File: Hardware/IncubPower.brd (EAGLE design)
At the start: 50 x 50 mm, 23 parts, among them T1 BT138-V, T2 BT138-V, X1 22-23-2041, X2 MKDSN1,5/2-5,08, X3 MKDSN1,5/2-5,08, X4 22-23-2021, X5 MKDSN1,5/2-5,08

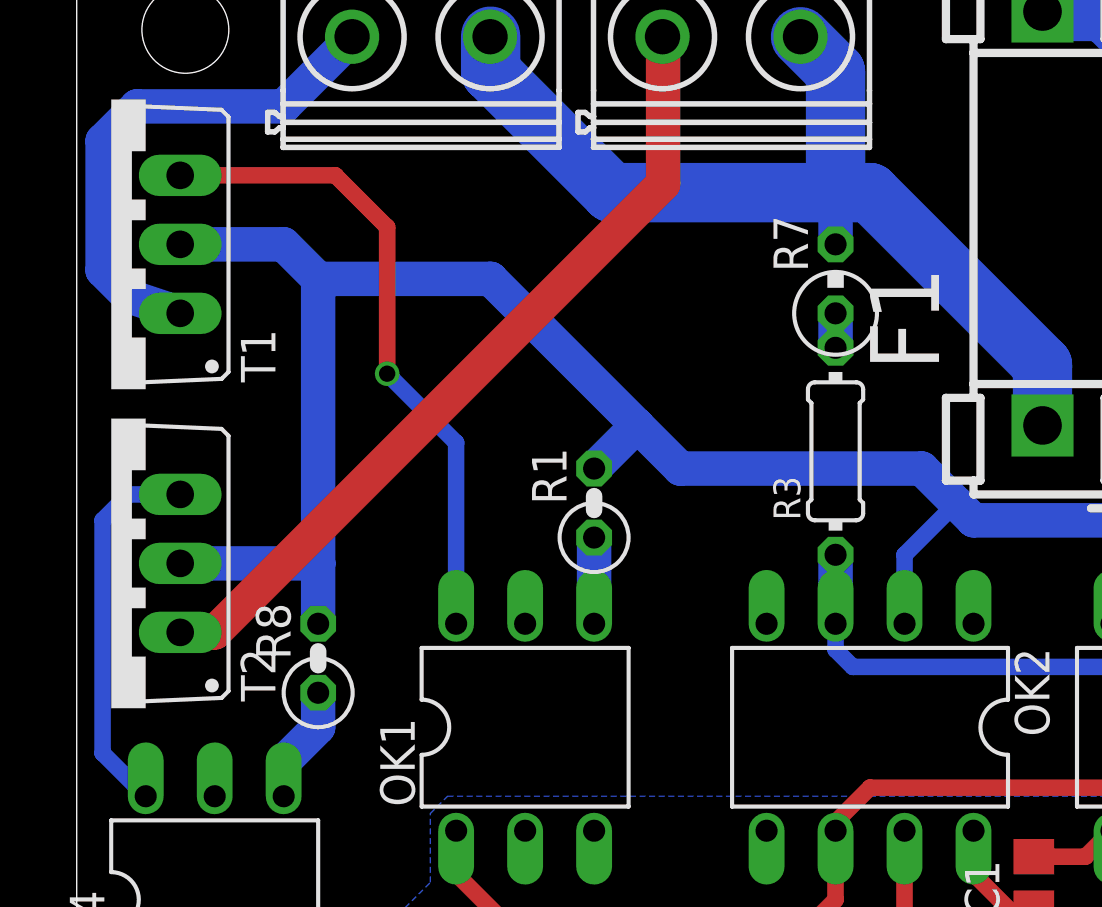
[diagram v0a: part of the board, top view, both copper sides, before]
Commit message: Release version
Version for production
- 3 buttons on control board
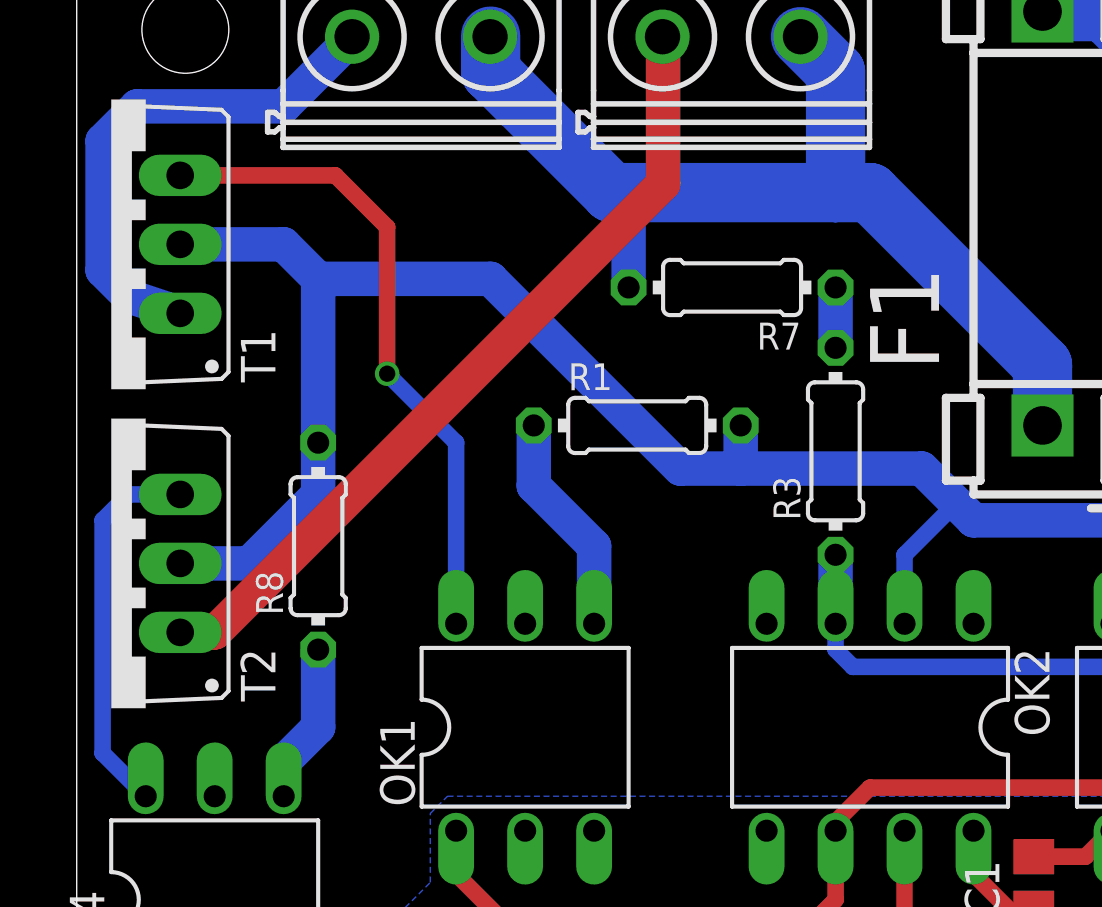
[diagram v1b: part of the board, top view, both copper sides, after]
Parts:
- R1, R8: device rcl:0207/2V -> rcl:0204/7
- R7: device resistor:0309V -> resistor:0204/7
- moved R8 4.13 mm to (8.89, 27.0)
- moved R7 3.82 mm to (24.1, 36.5), turned to 180 degrees
- moved R1 3.27 mm to (20.6, 31.4), turned to 0 degrees
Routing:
- net N$2: track 3.18 -> 8.22 mm
- net N$8: track 78.5 -> 74.1 mm
- net N$7: track 36.6 -> 38.3 mm
- net N$19: track 4.34 -> 5.92 mm
- net N$14: track 1.27 -> 2.22 mm
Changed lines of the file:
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@@
 <attribute name="OC_FARNELL" value="1505425" x="38.1" y="-19.05" size="1.778" layer="27" display="off"/>
 </element>
-<element name="R1" library="rcl" package="0207/2V" value="390" x="19.05" y="28.575" rot="R90"/>
+<element name="R1" library="rcl" package="0204/7" value="390" x="20.6375" y="31.4325"/>
 <element name="R2" library="rcl" package="R0805" value="330" x="16.51" y="11.43" rot="R90"/>
 <element name="X2" library="con-phoenix-508" package="MKDSN1,5/2-5,08" value="MKDSN1,5/2-5,08" x="12.7" y="45.72">
@@
 </element>
 <element name="R6" library="rcl" package="R0805" value="1 k [NP]" x="31.75" y="11.43" rot="R180"/>
-<element name="R7" library="resistor" package="0309V" value="68 k" x="27.94" y="36.83" rot="R90"/>
+<element name="R7" library="resistor" package="0204/7" value="68 k" x="24.13" y="36.5125" rot="R180"/>
 <element name="X4" library="con-molex" package="22-23-2021" value="22-23-2021" x="13.97" y="5.08">
 <attribute name="OC_NEWARK" value="25C3832" x="13.97" y="5.08" size="1.778" layer="27" display="off"/>
@@
 </element>
 <element name="T2" library="triac" package="TO220BV" value="BT138-V" x="1.27" y="26.3525" rot="R90"/>
-<element name="R8" library="rcl" package="0207/2V" value="390" x="8.89" y="22.86" rot="R90"/>
+<element name="R8" library="rcl" package="0204/7" value="390" x="8.89" y="26.9875" rot="R90"/>
 <element name="R9" library="rcl" package="R0805" value="330" x="8.89" y="5.08" rot="R90"/>
 <element name="X5" library="con-phoenix-508" package="MKDSN1,5/2-5,08" value="MKDSN1,5/2-5,08" x="24.13" y="45.72">
@@
 <contactref element="X5" pad="2"/>
 <wire x1="26.67" y1="45.7661" x2="26.6489" y2="45.745" width="1.27" layer="16"/>
-<wire x1="27.94" y1="38.1" x2="27.94" y2="40.005" width="1.27" layer="16"/>
-<wire x1="27.94" y1="40.005" x2="27.94" y2="41.91" width="0" layer="19" extent="1-16"/>
 <wire x1="27.94" y1="40.005" x2="27.94" y2="44.4539" width="2.1844" layer="16"/>
 <wire x1="27.94" y1="44.4539" x2="26.6489" y2="45.745" width="2.1844" layer="16"/>
@@
 <wire x1="15.24" y1="45.7661" x2="15.2189" y2="45.745" width="1.27" layer="16"/>
 <wire x1="15.24" y1="45.7661" x2="15.24" y2="44.45" width="2.1844" layer="16"/>
-<wire x1="27.6225" y1="42.2275" x2="27.94" y2="41.91" width="0" layer="19" extent="1-16"/>
 <wire x1="29.21" y1="40.005" x2="27.94" y2="40.005" width="2.1844" layer="16"/>
 <wire x1="15.24" y1="44.45" x2="19.685" y2="40.005" width="2.1844" layer="16"/>
-<wire x1="19.685" y1="40.005" x2="27.94" y2="40.005" width="2.1844" layer="16"/>
+<wire x1="19.685" y1="40.005" x2="20.6375" y2="40.005" width="2.1844" layer="16"/>
+<wire x1="20.6375" y1="40.005" x2="27.94" y2="40.005" width="2.1844" layer="16"/>
+<wire x1="20.32" y1="36.5125" x2="20.32" y2="39.6875" width="1.27" layer="16"/>
+<wire x1="20.32" y1="39.6875" x2="20.6375" y2="40.005" width="0.3048" layer="16"/>
 </signal>
 <signal name="N$8">
@@
 <wire x1="33.02" y1="27.94" x2="32.385" y2="28.575" width="1.27" layer="16"/>
 <wire x1="32.385" y1="28.575" x2="31.115" y2="29.845" width="1.27" layer="16"/>
-<wire x1="31.115" y1="29.845" x2="22.225" y2="29.845" width="1.27" layer="16"/>
-<wire x1="22.225" y1="29.845" x2="20.6375" y2="31.4325" width="1.27" layer="16"/>
-<wire x1="20.6375" y1="31.4325" x2="15.24" y2="36.83" width="1.27" layer="16"/>
+<wire x1="31.115" y1="29.845" x2="24.4475" y2="29.845" width="1.27" layer="16"/>
+<wire x1="24.4475" y1="29.845" x2="22.225" y2="29.845" width="1.27" layer="16"/>
+<wire x1="22.225" y1="29.845" x2="15.24" y2="36.83" width="1.27" layer="16"/>
 <wire x1="15.24" y1="36.83" x2="8.89" y2="36.83" width="1.27" layer="16"/>
-<wire x1="8.89" y1="24.13" x2="8.89" y2="26.3525" width="1.27" layer="16"/>
-<wire x1="8.89" y1="26.3525" x2="8.89" y2="36.83" width="1.27" layer="16"/>
-<wire x1="19.05" y1="29.845" x2="20.6375" y2="31.4325" width="1.27" layer="16"/>
+<wire x1="8.89" y1="30.7975" x2="8.89" y2="36.83" width="1.27" layer="16"/>
 <contactref element="T2" pad="T2"/>
 <contactref element="T1" pad="T2"/>
-<wire x1="3.81" y1="26.3525" x2="8.89" y2="26.3525" width="1.27" layer="16"/>
 <wire x1="3.81" y1="38.1" x2="7.62" y2="38.1" width="1.27" layer="16"/>
 <wire x1="7.62" y1="38.1" x2="8.89" y2="36.83" width="1.27" layer="16"/>
@@
 <wire x1="40.64" y1="24.13" x2="40.64" y2="26.67" width="0.6096" layer="16"/>
 <wire x1="40.64" y1="26.67" x2="39.37" y2="27.94" width="0.6096" layer="16"/>
+<wire x1="24.4475" y1="31.4325" x2="24.4475" y2="29.845" width="1.27" layer="16"/>
+<wire x1="3.81" y1="26.3525" x2="6.35" y2="26.3525" width="1.27" layer="16"/>
+<wire x1="8.89" y1="28.8925" x2="8.89" y2="30.7975" width="1.27" layer="16"/>
+<wire x1="6.35" y1="26.3525" x2="8.89" y2="28.8925" width="1.27" layer="16"/>
 </signal>
 <signal name="N$9">
@@
 <contactref element="OK1" pad="4"/>
 <contactref element="R1" pad="1"/>
-<wire x1="19.05" y1="27.305" x2="19.05" y2="24.13" width="1.27" layer="16"/>
+<wire x1="19.05" y1="24.13" x2="19.05" y2="26.9875" width="1.27" layer="16"/>
+<wire x1="19.05" y1="26.9875" x2="16.8275" y2="29.21" width="1.27" layer="16"/>
+<wire x1="16.8275" y1="29.21" x2="16.8275" y2="31.4325" width="1.27" layer="16"/>
 </signal>
 <signal name="N$11">
@@
 <contactref element="R3" pad="2"/>
 <contactref element="R7" pad="1"/>
-<wire x1="27.94" y1="35.56" x2="27.94" y2="34.29" width="1.27" layer="16"/>
+<wire x1="27.94" y1="36.5125" x2="27.94" y2="34.29" width="1.27" layer="16"/>
 </signal>
 <signal name="N$15">
@@
 <contactref element="OK4" pad="4"/>
 <contactref element="R8" pad="1"/>
-<wire x1="8.89" y1="21.59" x2="8.89" y2="20.32" width="1.27" layer="16"/>
+<wire x1="8.89" y1="23.1775" x2="8.89" y2="20.32" width="1.27" layer="16"/>
 <wire x1="8.89" y1="20.32" x2="7.62" y2="19.05" width="1.27" layer="16"/>
 <wire x1="7.62" y1="19.05" x2="7.62" y2="17.78" width="1.27" layer="16"/>
